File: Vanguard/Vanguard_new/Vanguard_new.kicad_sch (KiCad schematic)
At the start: 0 parts

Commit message: opened a new schematic
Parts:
- added C1: C, symbol Device:C
- added D1: PRTR5V0U2X, Package_TO_SOT_SMD:SOT-143, symbol Power_Protection:PRTR5V0U2X
- added J1: USB_B_Micro, symbol Connector:USB_B_Micro
- added J2: Conn_01x03_Pin, symbol Connector:Conn_01x03_Pin
- added R1: R, symbol Device:R
- added TP1: TestPoint, symbol Connector:TestPoint
- added U1: ATSAMD11D14A-M, Package_DFN_QFN:QFN-24-1EP_4x4mm_P0.5mm_EP2.6x2.6mm, symbol MCU_Microchip_SAMD:ATSAMD11D14A-M
- added U2: ATmega4809-A, Package_QFP:TQFP-48_7x7mm_P0.5mm, symbol MCU_Microchip_ATmega:ATmega4809-A
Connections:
- new net: C1.1, D1.2 (I/O1)
- new net: D1.4 (VCC), J1.1 (VBUS)
- new net: U2.14 (VCC), U2.42 (VCC)
- new net: U2.15 (GND), U2.29 (GND), U2.43 (GND)
- new net GND: C1.2, J1.5 (GND)

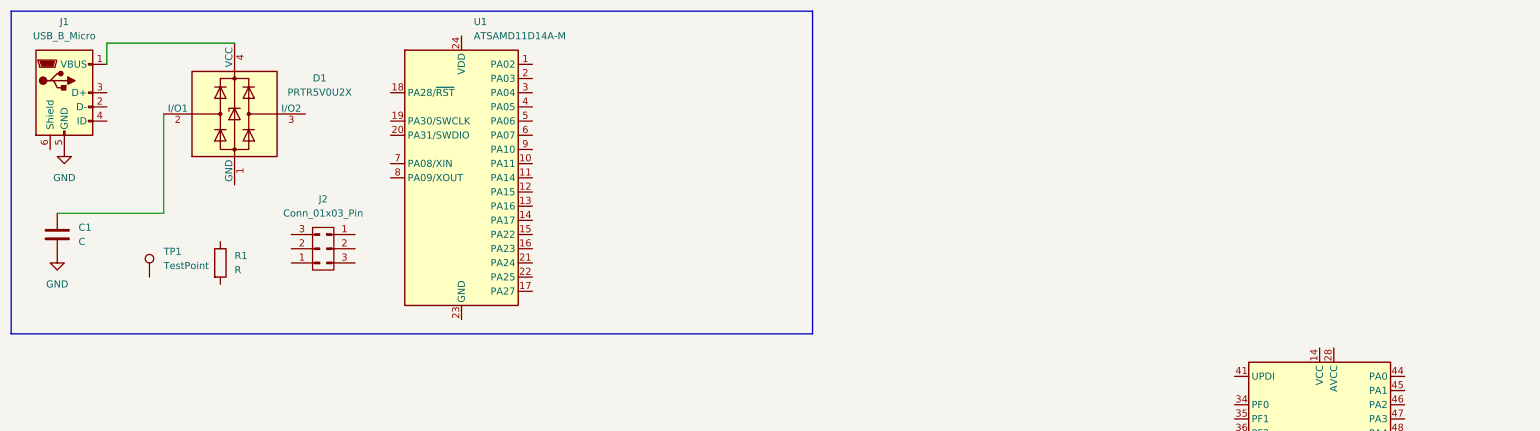
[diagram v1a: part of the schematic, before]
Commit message: opened the USB input section
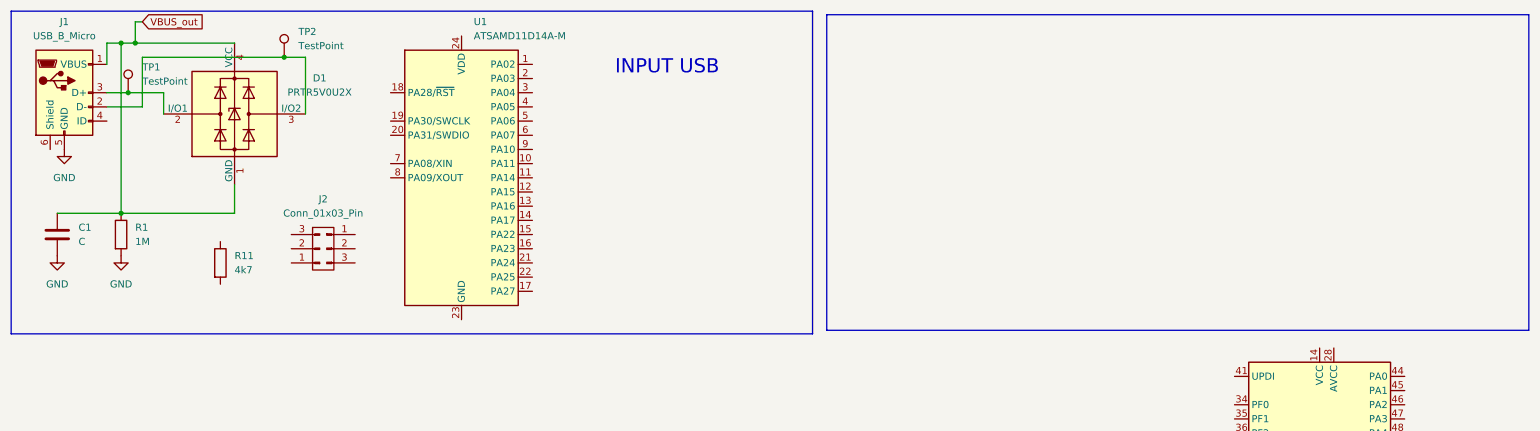
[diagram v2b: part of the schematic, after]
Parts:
- added R1: 1M, symbol Device:R
- added TP2: TestPoint, symbol Connector:TestPoint
- R11: renamed from R1; value R -> 4k7
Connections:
- net GND: now also R1.2
- net at D1.2 (I/O1): now also J1.3 (D+), TP1.1; no longer C1.1
- net VBUS_out: now reaches D1.4 (VCC), J1.1 (VBUS)
- net VBUS_out: now also C1.1, D1.1 (GND), R1.1
- net at J1.2 (D-): now also D1.3 (I/O2), TP2.1
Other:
- note added: "INPUT USB"
- moved on the sheet: TP1

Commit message: changes in the file exploror
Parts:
- added C2: 4u7, Capacitor_SMD:C_0402_1005Metric, symbol Device:C
- added C3: 0u1, Capacitor_SMD:C_0402_1005Metric, symbol Device:C
- added U3: LM34DM_NOPB, LM34DM_NOPB:SOIC127P599X175-8N, symbol LM34DM_NOPB:LM34DM_NOPB
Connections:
- net GND: now also C2.1, C3.1, U3.4 (GND)
- new net +5V: C2.2, C3.2, U3.8 (+VS)
- new net LM34DM_NOPB ANALOG OUT: U3.1 (VOUT)
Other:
- note added: "POWER STABILIZATION"
- note added: "SENSORS"
- moved on the sheet: U2

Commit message: Input usb finished
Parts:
- added D2, D3: LED, symbol Device:LED
- added D4: DNP, symbol Device:D_Zener
- added Q1, Q2, Q3: BSS138, Package_TO_SOT_SMD:SOT-23, symbol Transistor_FET:BSS138
- added R10, R12, R13, R2, R6, R7, R9: 4k7, symbol Device:R
- added R3, R4: 330, symbol Device:R
- added R5: 0, symbol Device:R
- added R8: DNP, symbol Device:R
- C1: value C -> 4n7
- J1: symbol Connector:USB_B_Micro -> Connector:USB_C_Plug_USB2.0
- J2: symbol Connector:Conn_01x03_Pin -> Connector_Generic:Conn_02x03_Odd_Even
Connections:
- net GND: now also J1.A1 (GND), J1.A12 (GND), J1.B1 (GND), J1.B12 (GND), J1.S1 (SHIELD), J2.5 (Pin_5), U1.23 (GND); no longer J1.5 (GND)
- net VBUS_out: now also J1.A4 (VBUS), J1.A9 (VBUS), J1.B4 (VBUS), J1.B9 (VBUS); no longer J1.1 (VBUS)
- net +3.3V: now reaches R11.1
- net +3.3V: now also J2.1 (Pin_1), U1.24 (VDD), D4.1 (K), Q1.1 (G), Q2.1 (G), Q3.1 (G), R10.1, R12.1, R13.1, R2.1, R3.1, R4.1, R6.1, R7.1, R9.1
- net at R11.2: now also J2.6 (Pin_6), U1.18 (PA28/~{RST})
- net at D1.2 (I/O1), TP1.1: now also J1.A6 (D+), U1.22 (PA25); no longer J1.3 (D+)
- net RX_UPDI: now reaches U1.11 (PA14)
- net RX_UPDI: now also U1.12 (PA15), D4.2 (A), Q1.2 (S), R5.1, R5.2, R6.2, R8.1
- net at U1.15 (PA22): now also D3.1 (K), Q2.2 (S), R10.2
- net at U1.16 (PA23): now also D2.1 (K), Q3.2 (S), R9.2
- net at U1.19 (PA30/SWCLK): now also J2.3 (Pin_3), R2.2
- net at U1.20 (PA31/SWDIO): now also J2.2 (Pin_2)
- net at U1.21 (PA24): now also D1.3 (I/O2), J1.A7 (D-), TP2.1
- net TX0: now reaches U2.8 (PB4)
- net TX0: now also Q2.3 (D), R13.2
- net RX0: now reaches U2.9 (PB5)
- net RX0: now also Q3.3 (D), R12.2
- new net: D3.2 (A), R3.2
- new net: D2.2 (A), R4.2
- new net UPDI: J2.4 (Pin_4), Q1.3 (D), R7.2, R8.2
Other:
- moved on the sheet: C1, D1, R1, R11, TP1, TP2, U1

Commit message: power stabilization done.
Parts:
- added C4, C5: 22u, symbol Device:C
- added C6: 1u, symbol Device:C
- added D5: GREEN, symbol Device:LED
- added D6: PMEG6020ER, Diode_SMD:Nexperia_CFP3_SOD-123W, symbol Diode:PMEG6020ER
- added R14, R15: 100k, symbol Device:R
- added R16: 19k1, symbol Device:R
- added R17: 330R, symbol Device:R
- added U4: AP2112K-3.3, Package_TO_SOT_SMD:SOT-23-5, symbol Regulator_Linear:AP2112K-3.3
- added U5: MPM3610AGQV-P, MPM3610AGQV-P:CONV_MPM3620AGQV-P, symbol MPM3610AGQV-P:MPM3610AGQV-P
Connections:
- net +3.3V: now also C6.1, R17.1, U4.5 (VOUT)
- net GND: now also U2.15 (GND), U2.29 (GND), U2.43 (GND), C4.2, C5.2, C6.2, D5.1 (K), D6.1 (K), R16.2, U4.2 (GND), U5. (SW), U5.3 (AGND)
- net VBUS_out: now also D6.2 (A)
- new net: C4.1, R14.1, U5.16 (VIN)
- new net: R14.2, U5.17 (EN)
- new net: R15.2, R16.1, U5.1 (FB)
- new net: C5.1, R15.1, U4.1 (VIN), U4.3 (EN), U5. (SW)
- new net: D5.2 (A), R17.2
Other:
- moved on the sheet: U2

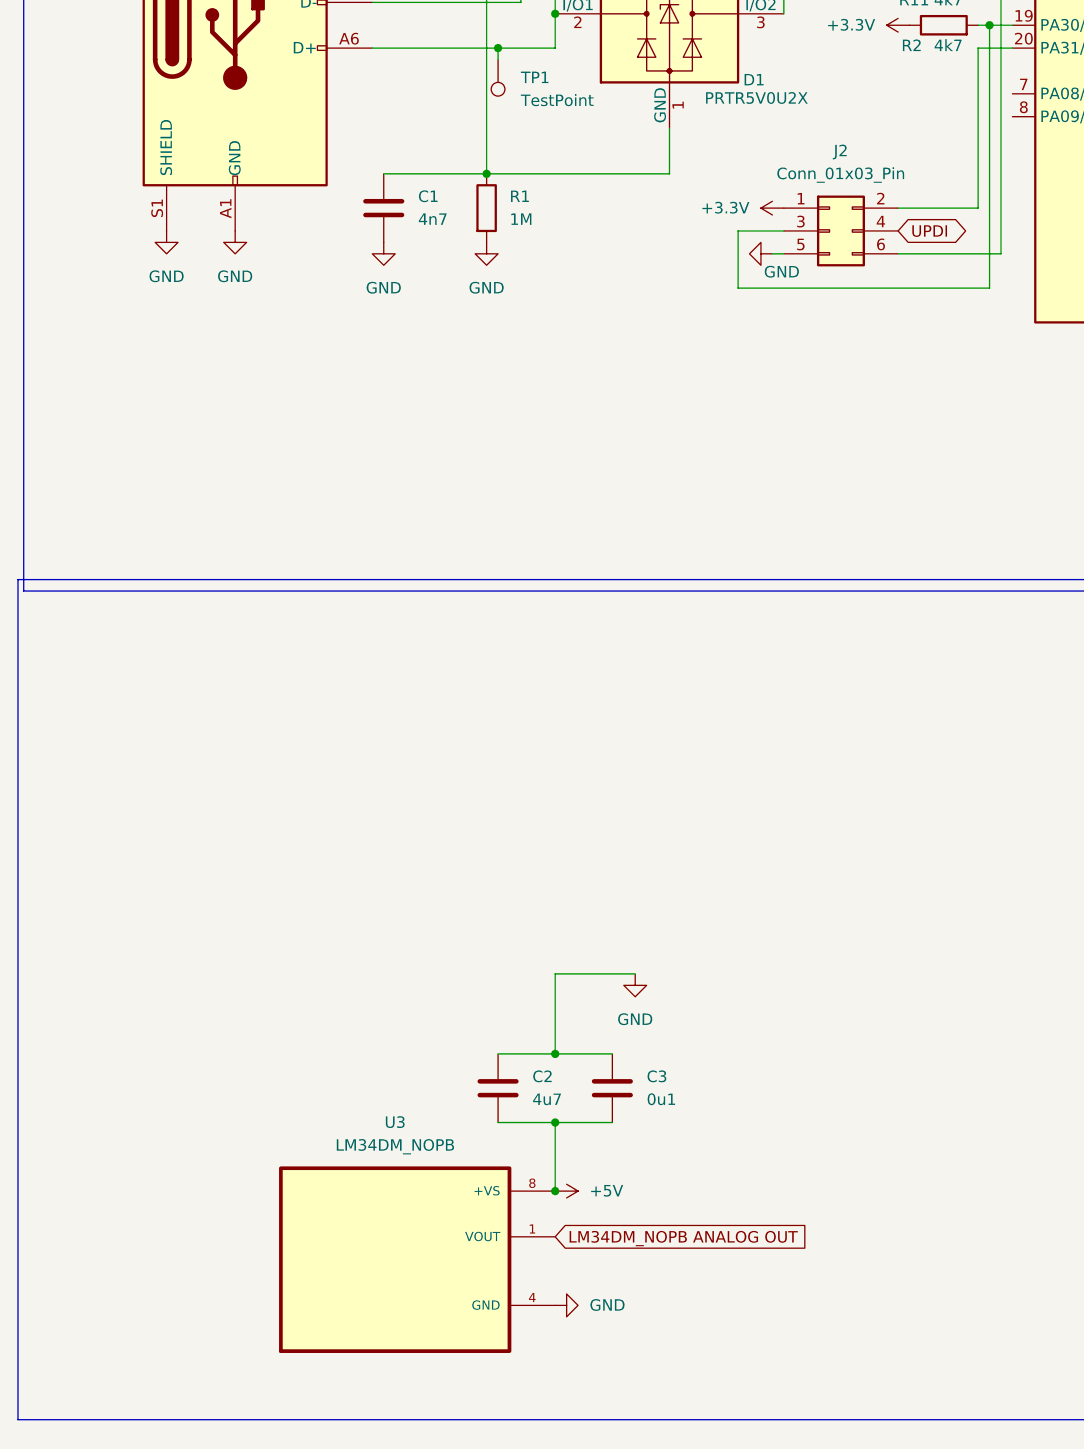
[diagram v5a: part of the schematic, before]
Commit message: +temp +9axis
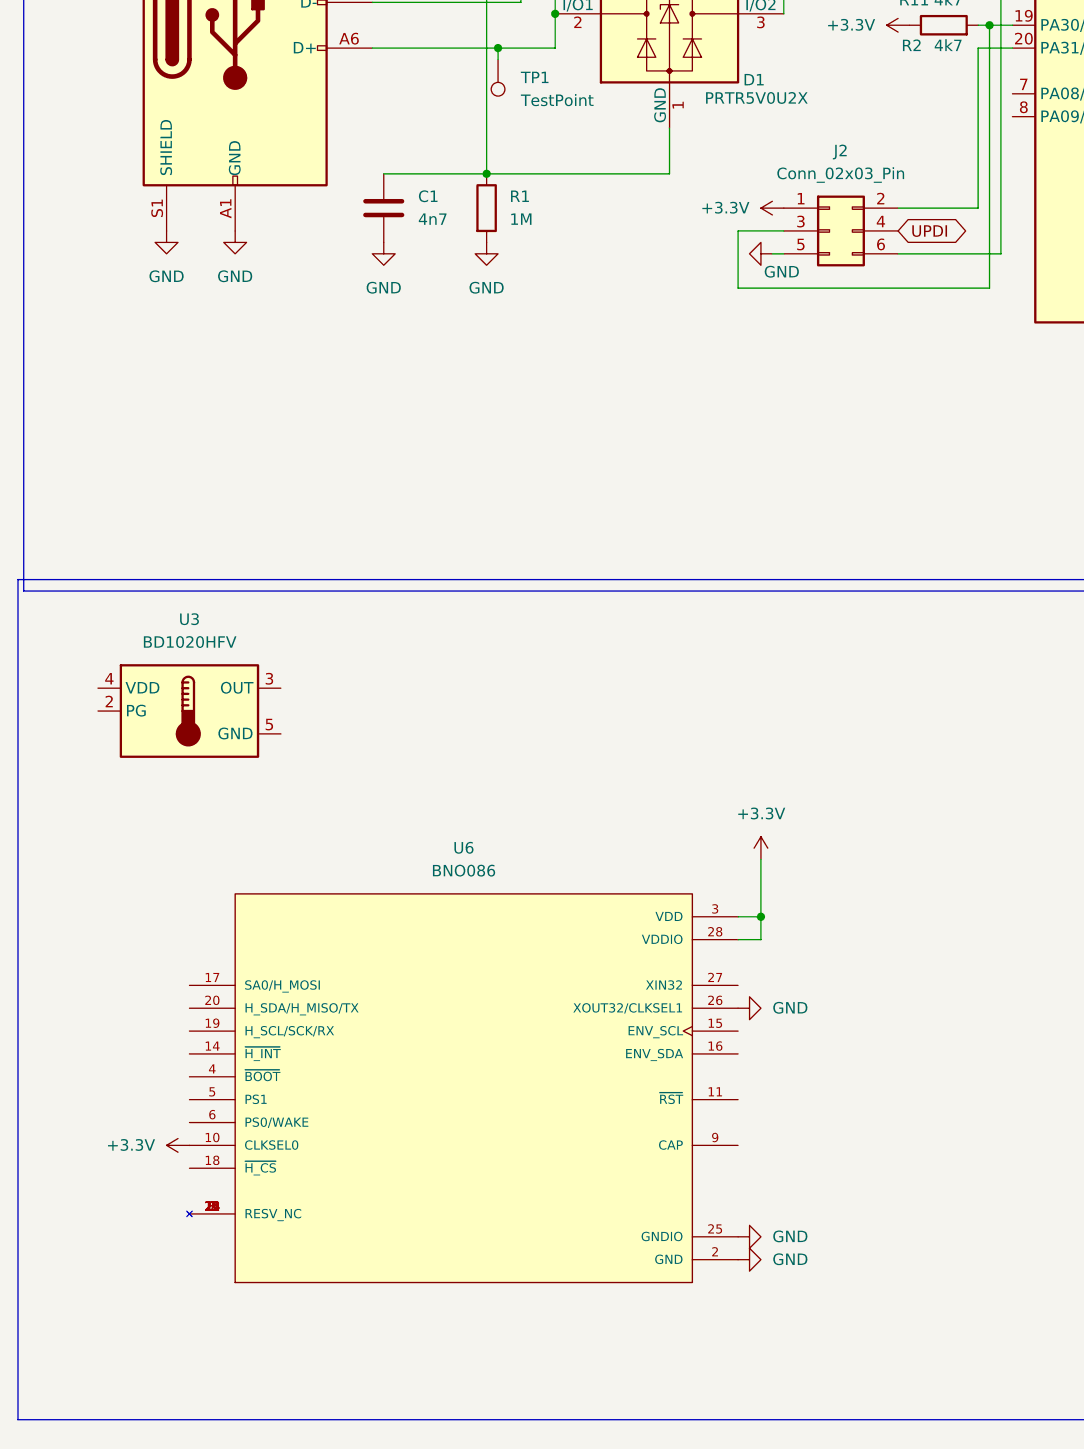
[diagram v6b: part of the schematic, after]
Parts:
- removed C2: 4u7, Capacitor_SMD:C_0402_1005Metric, symbol Device:C
- removed C3: 0u1, Capacitor_SMD:C_0402_1005Metric, symbol Device:C
- removed U3: LM34DM_NOPB, LM34DM_NOPB:SOIC127P599X175-8N, symbol LM34DM_NOPB:LM34DM_NOPB
- added U3: BD1020HFV, Package_TO_SOT_SMD:HVSOF5, symbol Sensor_Temperature:BD1020HFV
- added U6: BNO086, BNO086:IC_BNO086, symbol BNO086:BNO086
- J2: value Conn_01x03_Pin -> Conn_02x03_Pin
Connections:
- net +3.3V: now also U6.10 (CLKSEL0), U6.28 (VDDIO), U6.3 (VDD)
- net GND: now also U6.2 (GND), U6.25 (GNDIO), U6.26 (XOUT32/CLKSEL1)
- new net: U6.1 (RESV_NC), U6.12 (RESV_NC), U6.13 (RESV_NC), U6.21 (RESV_NC), U6.22 (RESV_NC), U6.23 (RESV_NC), U6.24 (RESV_NC), U6.7 (RESV_NC), U6.8 (RESV_NC)
